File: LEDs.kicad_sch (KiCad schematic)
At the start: 0 parts

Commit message: USB and PWR sch
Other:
- title: (none) -> LEDs
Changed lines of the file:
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@@
 	(generator_version "8.0")
 	(paper "A4")
+	(title_block
+		(title "LEDs")
+	)
 )

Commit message: finished sch? (need P/Ns)
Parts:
- added D7: DANGER, symbol Device:LED
- added R10: TODO, symbol Device:R
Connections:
- new net: D7.2 (A), R10.2
- new net GND: D7.1 (K)
- new net LED_0: R10.1
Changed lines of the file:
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@@
 		(title "LEDs")
 	)
+	(wire
+		(pts
+			(xy 19.05 22.86) (xy 19.05 25.4)
+		)
+		(stroke
+			(width 0)
+			(type default)
+		)
+	)
+	(wire
+		(pts
+			(xy 19.05 33.02) (xy 19.05 35.56)
+		)
+		(stroke
+			(width 0)
+			(type default)
+		)
+	)
+	(wire
+		(pts
+			(xy 19.05 43.18) (xy 19.05 45.72)
+		)
+		(stroke
+			(width 0)
+			(type default)
+		)
+	)
+	(hierarchical_label "LED_0"
+		(shape input)
+		(at 19.05 22.86 90)
+		(fields_autoplaced yes)
+		(effects
+			(font
+				(size 1.27 1.27)
+			)
+			(justify left)
+		)
+	)
+	(symbol
+		(lib_id "power:GND")
+		(at 19.05 45.72 0)
+		(unit 1)
+		(exclude_from_sim no)
+		(in_bom yes)
+		(on_board yes)
+		(dnp no)
+		(fields_autoplaced yes)
+		(property "Reference" "#PWR028"
+			(at 19.05 52.07 0)
+			(effects
+				(font
+					(size 1.27 1.27)
+				)
+				(hide yes)
+			)
+		)
+		(property "Value" "GND"
+			(at 19.05 50.8 0)
+			(effects
+				(font
+					(size 1.27 1.27)
+				)
+			)
+		)
+		(property "Footprint" ""
+			(at 19.05 45.72 0)
+			(effects
+				(font
+					(size 1.27 1.27)
+				)
+				(hide yes)
+			)
+		)
+		(property "Datasheet" ""
+			(at 19.05 45.72 0)
+			(effects
+				(font
+					(size 1.27 1.27)
+				)
+				(hide yes)
+			)
+		)
+		(property "Description" "Power symbol creates a global label with name \"GND\" , ground"
+			(at 19.05 45.72 0)
+			(effects
+				(font
+					(size 1.27 1.27)
+				)
+				(hide yes)
+			)
+		)
+		(pin "1"
+		)
+		(instances
+			(project ""
+				(path "/0204cec0-d71e-48a7-8736-ccb0d3e9b02c/d1e7b685-9c83-4c15-8db3-0beed5698ce7/8184fca5-5229-48fa-bbef-82ce17fecaf5"
+					(reference "#PWR028")
+					(unit 1)
+				)
+			)
+		)
+	)
+	(symbol
+		(lib_id "Device:LED")
+		(at 19.05 39.37 90)
+		(unit 1)
+		(exclude_from_sim no)
+		(in_bom yes)
+		(on_board yes)
+		(dnp no)
+		(fields_autoplaced yes)
+		(property "Reference" "D7"
+			(at 22.86 39.6874 90)
+			(effects
+				(font
+					(size 1.27 1.27)
+				)
+				(justify right)
+			)
+		)
+		(property "Value" "DANGER"
+			(at 22.86 42.2274 90)
+			(effects
+				(font
+					(size 1.27 1.27)
+				)
+				(justify right)
+			)
+		)
+		(property "Footprint" ""
+			(at 19.05 39.37 0)
+			(effects
+				(font
+					(size 1.27 1.27)
+				)
+				(hide yes)
+			)
+		)
+		(property "Datasheet" "~"
+			(at 19.05 39.37 0)
+			(effects
+				(font
+					(size 1.27 1.27)
+				)
+				(hide yes)
+			)
+		)
+		(property "Description" "Light emitting diode"
+			(at 19.05 39.37 0)
+			(effects
+				(font
+					(size 1.27 1.27)
+				)
+				(hide yes)
+			)
+		)
+		(pin "2"
+		)
+		(pin "1"
+		)
+		(instances
+			(project "esp32-devboard"
+				(path "/0204cec0-d71e-48a7-8736-ccb0d3e9b02c/d1e7b685-9c83-4c15-8db3-0beed5698ce7/8184fca5-5229-48fa-bbef-82ce17fecaf5"
+					(reference "D7")
+					(unit 1)
+				)
+			)
+		)
+	)
+	(symbol
+		(lib_id "Device:R")
+		(at 19.05 29.21 0)
+		(unit 1)
+		(exclude_from_sim no)
+		(in_bom yes)
+		(on_board yes)
+		(dnp no)
+		(fields_autoplaced yes)
+		(property "Reference" "R10"
+			(at 21.59 27.9399 0)
+			(effects
+				(font
+					(size 1.27 1.27)
+				)
+				(justify left)
+			)
+		)
+		(property "Value" "TODO"
+			(at 21.59 30.4799 0)
+			(effects
+				(font
+					(size 1.27 1.27)
+				)
+				(justify left)
+			)
+		)
+		(property "Footprint" ""
+			(at 17.272 29.21 90)
+			(effects
+				(font
+					(size 1.27 1.27)
+				)
+				(hide yes)
+			)
+		)
+		(property "Datasheet" "~"
+			(at 19.05 29.21 0)
+			(effects
+				(font
+					(size 1.27 1.27)
+				)
+				(hide yes)
+			)
+		)
+		(property "Description" "Resistor"
+			(at 19.05 29.21 0)
+			(effects
+				(font
+					(size 1.27 1.27)
+				)
+				(hide yes)
+			)
+		)
+		(pin "1"
+		)
+		(pin "2"
+		)
+		(instances
+			(project ""
+				(path "/0204cec0-d71e-48a7-8736-ccb0d3e9b02c/d1e7b685-9c83-4c15-8db3-0beed5698ce7/8184fca5-5229-48fa-bbef-82ce17fecaf5"
+					(reference "R10")
+					(unit 1)
+				)
+			)
+		)
+	)
 )

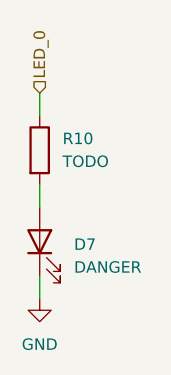
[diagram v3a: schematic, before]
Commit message: add P/N
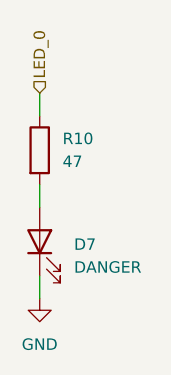
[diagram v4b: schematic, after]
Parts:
- D7: P/N (none) -> HSML-C191
- R10: value TODO -> 47; P/N (none) -> MCT06030C4709FP500
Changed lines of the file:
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@@
+			)
+		)
+		(property "P/N" "HSML-C191"
+			(at 19.05 39.37 90)
+			(effects
+				(font
+					(size 1.27 1.27)
+				)
+				(hide yes)
+			)
+		)
+		(property "Field6" ""
+			(at 19.05 39.37 90)
+			(effects
+				(font
+					(size 1.27 1.27)
+				)
+				(hide yes)
 			)
 		)
@@
 			)
 		)
-		(property "Value" "TODO"
+		(property "Value" "47"
 			(at 21.59 30.4799 0)
 			(effects
@@
 			(at 19.05 29.21 0)
 			(effects
+				(font
+					(size 1.27 1.27)
+				)
+				(hide yes)
+			)
+		)
+		(property "P/N" "MCT06030C4709FP500 "
+			(at 19.05 29.21 0)
+			(effects

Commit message: assign footprints
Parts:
- D7: footprint (none) -> LED_SMD:LED_0603_1608Metric
- R10: footprint (none) -> Resistor_SMD:R_0603_1608Metric
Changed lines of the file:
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@@
 			)
 		)
-		(property "Footprint" ""
+		(property "Footprint" "LED_SMD:LED_0603_1608Metric"
 			(at 19.05 39.37 0)
 			(effects
@@
 			)
 		)
-		(property "Footprint" ""
+		(property "Footprint" "Resistor_SMD:R_0603_1608Metric"
 			(at 17.272 29.21 90)
 			(effects
